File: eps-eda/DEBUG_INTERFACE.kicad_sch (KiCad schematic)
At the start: 12 parts, among them J4 Conn_01x05_Female

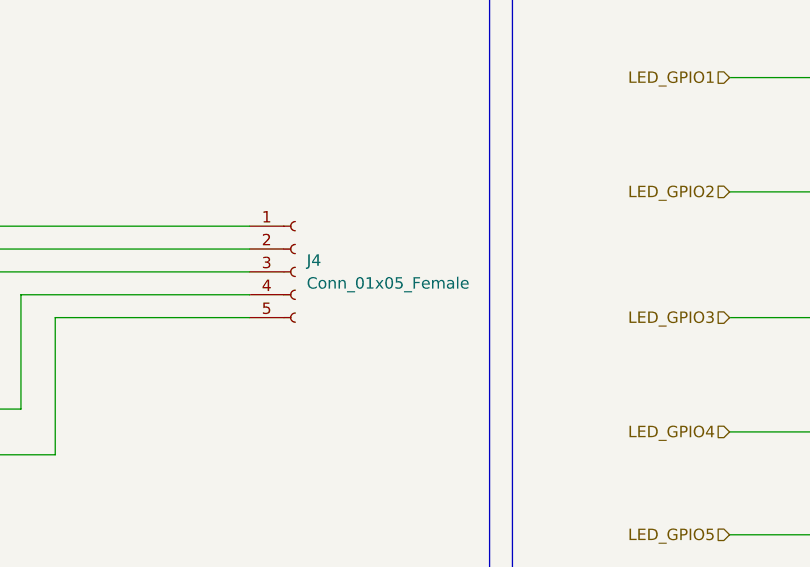
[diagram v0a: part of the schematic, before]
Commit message: rev 0.2 update
added 90deg pic adapter to include an edge cutout.

changed footprint of fuel gauge to implement ALRT signal.

rotated battery connector to better implement with the battery board.

Co-Authored-By: ajbrannigan <91212154+ajbrannigan@users.noreply.github.com>
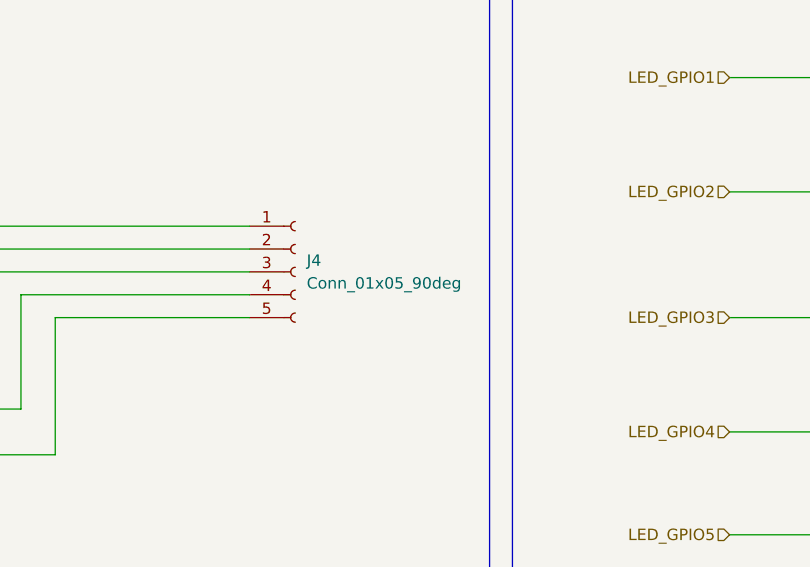
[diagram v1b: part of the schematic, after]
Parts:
- J4: value Conn_01x05_Female -> Conn_01x05_90deg; footprint Connector_PinSocket_2.54mm:PinSocket_1x05_P2.54mm_Vertical -> Connector_PinHeader_2.54mm:PinHeader_1x05_P2.54mm_Horizontal
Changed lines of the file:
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@@
       (effects (font (size 1.27 1.27)) (justify left))
     )
-    (property "Value" "Conn_01x05_Female" (id 1) (at 157.48 93.9799 0)
+    (property "Value" "Conn_01x05_90deg" (id 1) (at 157.48 93.9799 0)
       (effects (font (size 1.27 1.27)) (justify left))
     )
-    (property "Footprint" "Connector_PinSocket_2.54mm:PinSocket_1x05_P2.54mm_Vertical" (id 2) (at 156.21 92.71 0)
+    (property "Footprint" "Connector_PinHeader_2.54mm:PinHeader_1x05_P2.54mm_Horizontal" (id 2) (at 156.21 92.71 0)
       (effects (font (size 1.27 1.27)) hide)
     )
